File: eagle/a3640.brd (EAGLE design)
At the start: 207 x 98 mm, 9 parts, among them IC1 MC68040RC, U214 74FCT543, U215 74FCT543, U216 74FCT543, U217 74FCT543, U218 74FCT543, U219 74FCT543, U220 74FCT543, U221 74FCT543

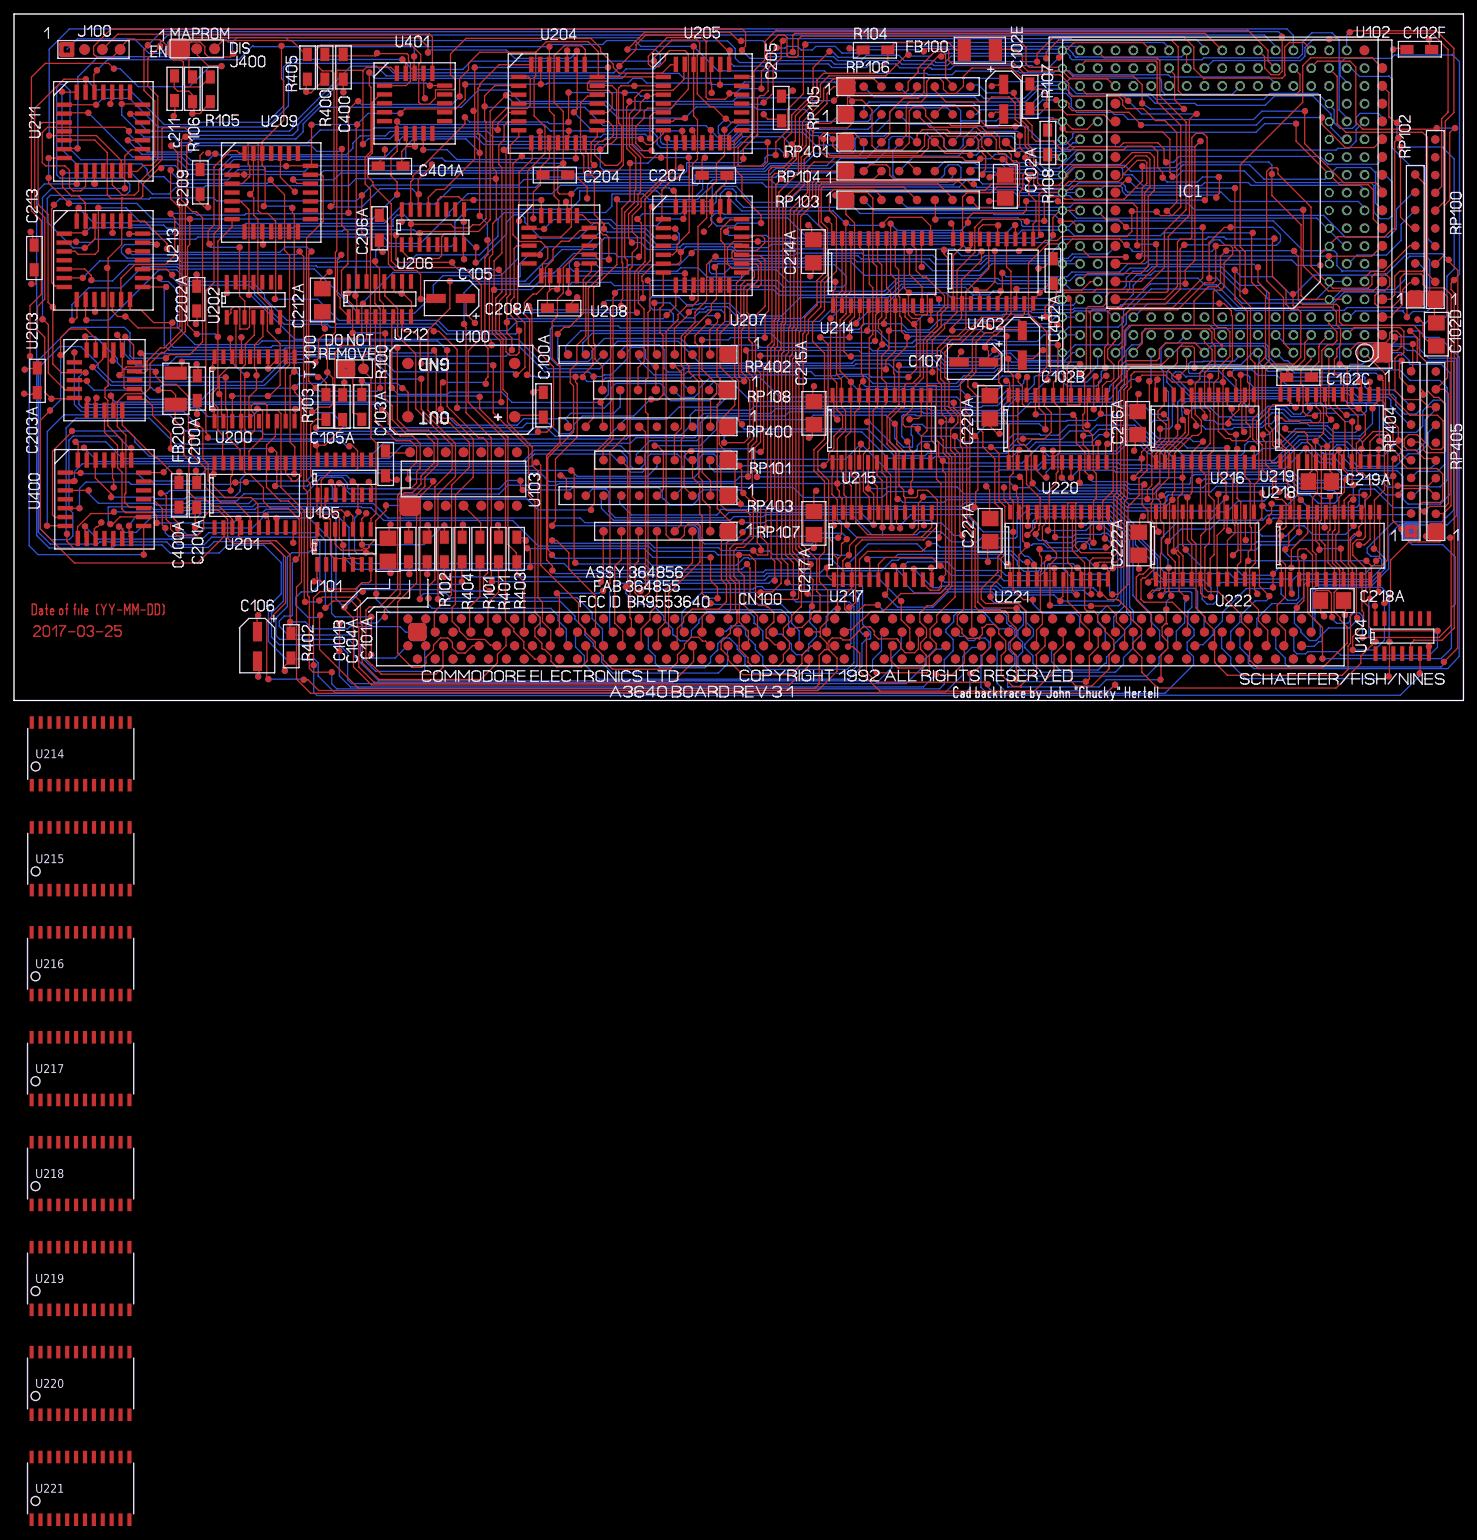
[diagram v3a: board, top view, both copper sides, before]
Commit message: footprint update and parts placement
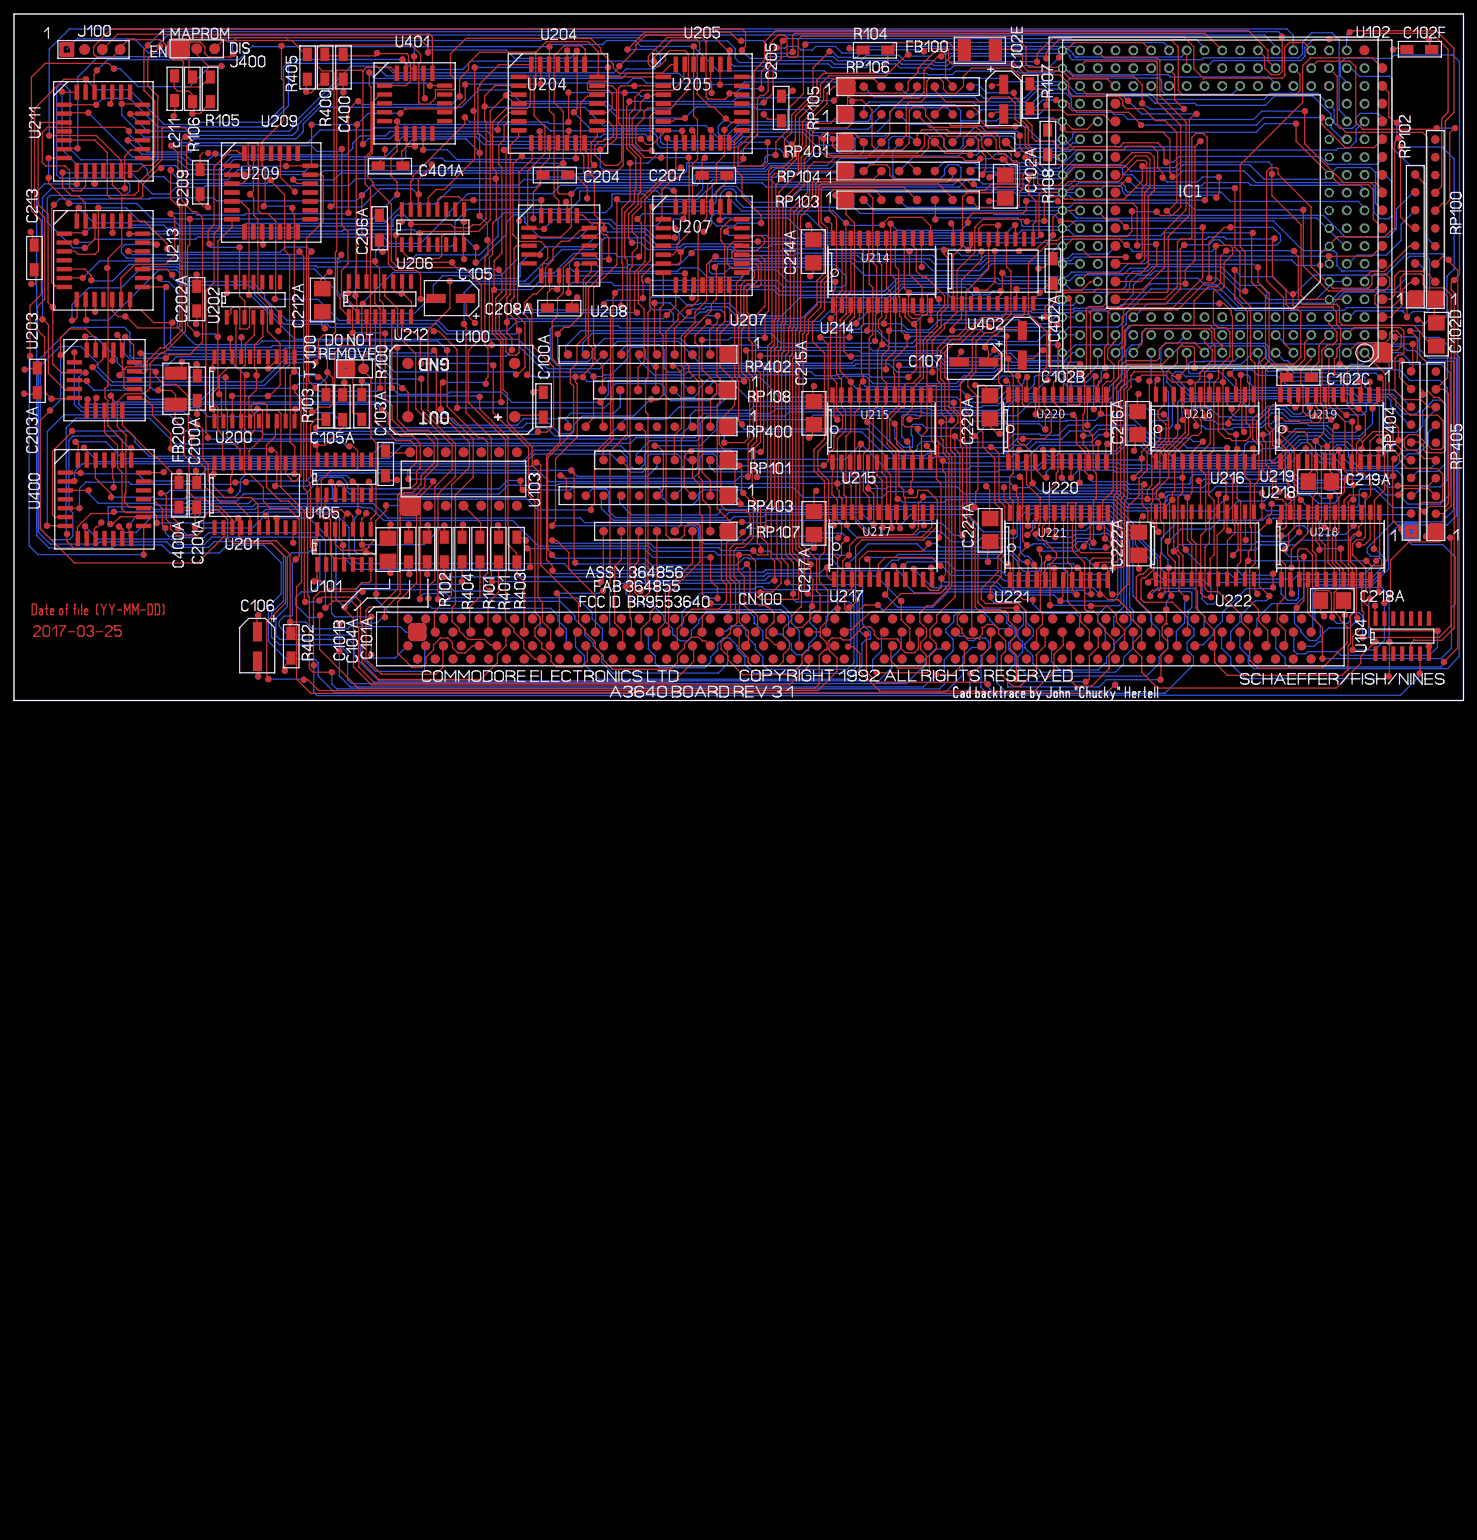
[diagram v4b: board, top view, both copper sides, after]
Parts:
- added U204, U205, U207, U209: GAL22V10, a3640_edu_v0.1:GAL22V10
- U214, U215, U216, U217, U218, U219, U220, U221: value 74FCT543 -> 74FCT543SOIC24; device terriblefire:SOIC24L -> terriblefire:74FCT543A
- moved U219 215.8 mm to (187.9, 38.9)
- moved U218 199.7 mm to (188.0, 22.0)
- moved U220 195.1 mm to (149.0, 38.9)
- moved U221 193.9 mm to (149.2, 21.9)
- moved U216 177.9 mm to (170.1, 38.9)
- moved U217 136.8 mm to (124.2, 22.1)
- moved U214 133.5 mm to (123.9, 61.2)
- moved U215 129.8 mm to (123.9, 38.8)
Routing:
- net VCC: track 0.00 -> 81.3 mm
- net S$173: track 31.8 -> 0.00 mm
- net S$129: track 23.1 -> 0.00 mm
- net S$405: track 11.7 -> 0.00 mm
- net S$400: track 9.98 -> 0.00 mm
- net S$172: track 4.69 -> 0.00 mm
